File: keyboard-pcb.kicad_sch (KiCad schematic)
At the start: 24 parts, among them J1 Conn_01x05, J2 USB_C_Receptacle_USB2.0_16P, SW1 BOOT, SW2 RESET, U1 STM32F072CBTx, U2 74AHCT1G125, U3 XC6206PxxxMR

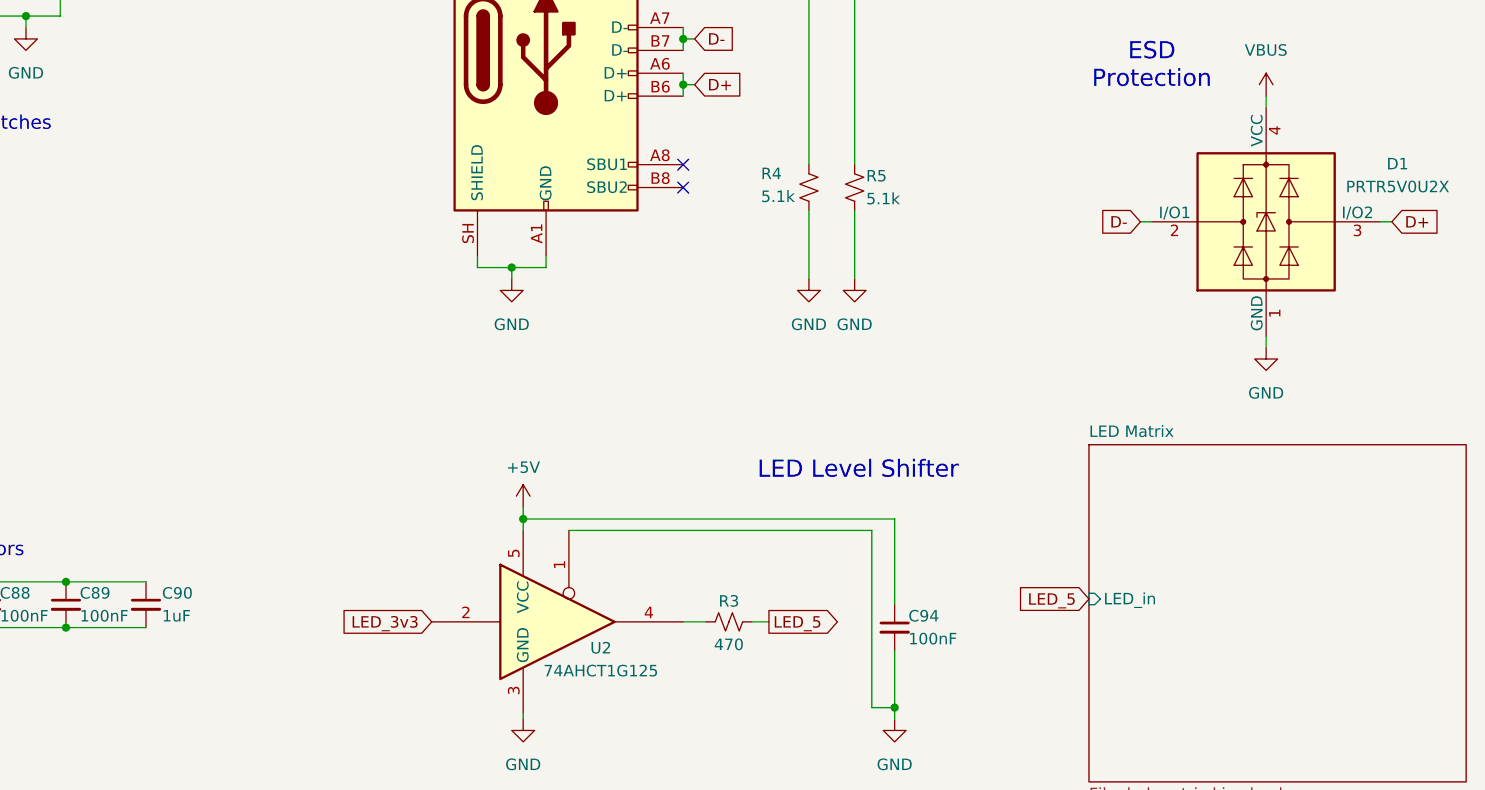
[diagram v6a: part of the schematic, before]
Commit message: usb and ldo routing
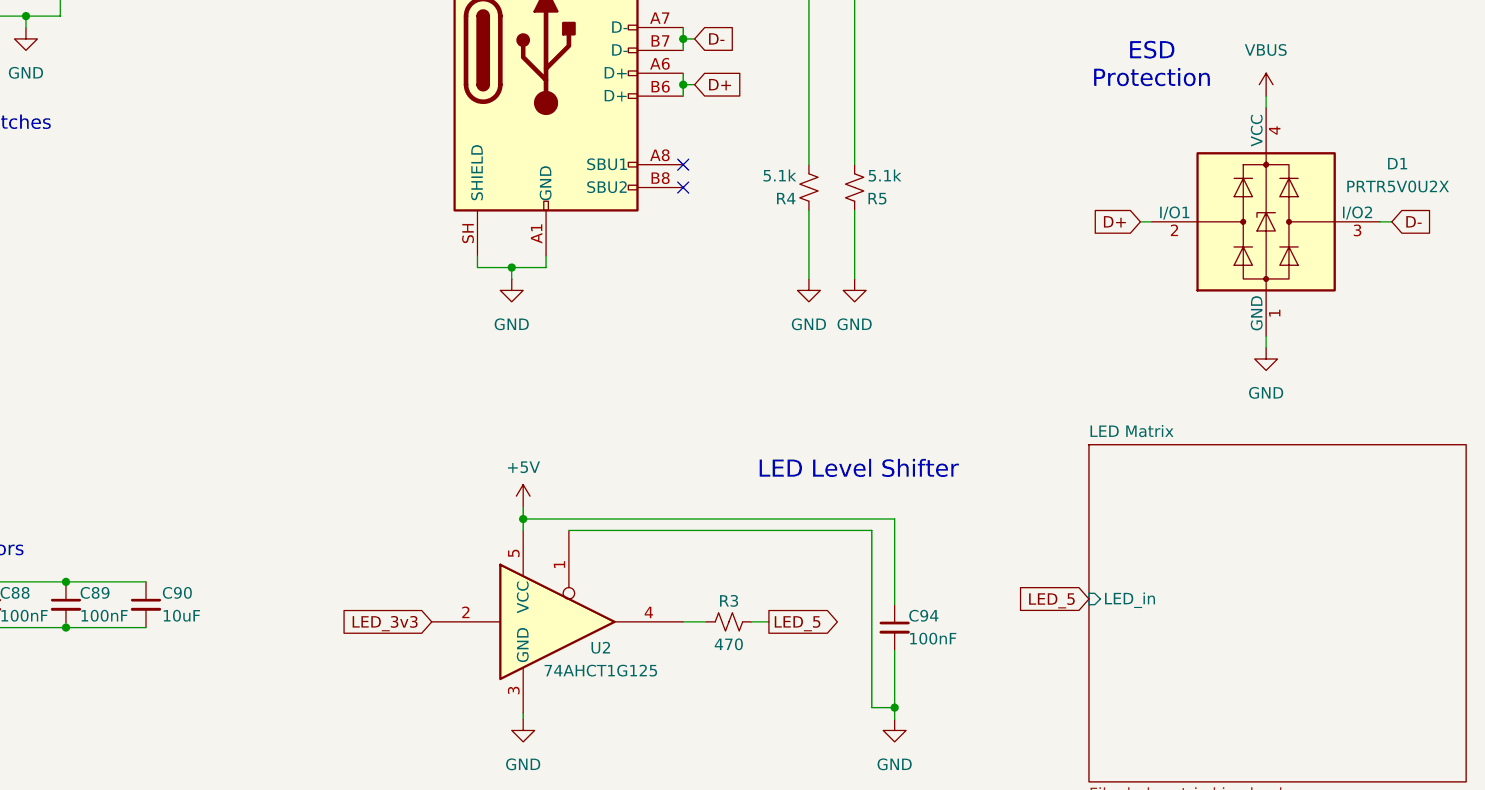
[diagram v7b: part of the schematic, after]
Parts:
- C90: value 1uF -> 10uF
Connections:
- net D+: now also D1.2 (I/O1); no longer D1.3 (I/O2)
- net D-: now also D1.3 (I/O2); no longer D1.2 (I/O1)
- net GND: now also R4.2, R5.1; no longer R4.1, R5.2
- net at J2.A5 (CC1): now also R5.2; no longer R5.1
- net at J2.B5 (CC2): now also R4.1; no longer R4.2
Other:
- moved on the sheet: R4, R5
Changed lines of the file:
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@@
 	(global_label "D-"
 		(shape input)
-		(at 247.015 66.04 180)
-		(fields_autoplaced yes)
-		(effects
-			(font
-				(size 1.27 1.27)
-			)
-			(justify right)
-		)
-		(property "Intersheetrefs" "${INTERSHEET_REFS}"
-			(at 241.1874 66.04 0)
-			(hide yes)
-			(show_name no)
-			(do_not_autoplace no)
-			(effects
-				(font
-					(size 1.27 1.27)
-				)
-				(justify right)
+		(at 274.955 66.04 0)
+		(fields_autoplaced yes)
+		(effects
+			(font
+				(size 1.27 1.27)
+			)
+			(justify left)
+		)
+		(property "Intersheetrefs" "${INTERSHEET_REFS}"
+			(at 280.7826 66.04 0)
+			(hide yes)
+			(show_name no)
+			(do_not_autoplace no)
+			(effects
+				(font
+					(size 1.27 1.27)
+				)
+				(justify left)
 			)
 		)
@@
 	(global_label "D+"
 		(shape input)
-		(at 274.955 66.04 0)
-		(fields_autoplaced yes)
-		(effects
-			(font
-				(size 1.27 1.27)
-			)
-			(justify left)
-		)
-		(property "Intersheetrefs" "${INTERSHEET_REFS}"
-			(at 280.7826 66.04 0)
-			(hide yes)
-			(show_name no)
-			(do_not_autoplace no)
-			(effects
-				(font
-					(size 1.27 1.27)
-				)
-				(justify left)
+		(at 247.015 66.04 180)
+		(fields_autoplaced yes)
+		(effects
+			(font
+				(size 1.27 1.27)
+			)
+			(justify right)
+		)
+		(property "Intersheetrefs" "${INTERSHEET_REFS}"
+			(at 241.1874 66.04 0)
+			(hide yes)
+			(show_name no)
+			(do_not_autoplace no)
+			(effects
+				(font
+					(size 1.27 1.27)
+				)
+				(justify right)
 			)
 		)
@@
 	(symbol
 		(lib_id "Device:R_Small_US")
-		(at 215.265 62.23 0)
+		(at 215.265 62.23 180)
 		(unit 1)
 		(body_style 1)
@@
 		(dnp no)
 		(property "Reference" "R5"
-			(at 216.535 60.96 0)
+			(at 218.948 63.5 0)
 			(show_name no)
 			(do_not_autoplace no)
@@
 		)
 		(property "Value" "5.1k"
-			(at 216.535 63.5 0)
+			(at 220.472 60.96 0)
 			(show_name no)
 			(do_not_autoplace no)
@@
 	(symbol
 		(lib_id "Device:R_Small_US")
-		(at 210.185 62.23 180)
+		(at 210.185 62.23 0)
 		(unit 1)
 		(body_style 1)
@@
 		(dnp no)
 		(property "Reference" "R4"
-			(at 204.851 60.706 0)
+			(at 208.788 63.5 0)
 			(show_name no)
 			(do_not_autoplace no)
@@
 		)
 		(property "Value" "5.1k"
-			(at 204.851 63.246 0)
+			(at 208.788 60.96 0)
 			(show_name no)
 			(do_not_autoplace no)
@@
 			)
 		)
-		(property "Value" "1uF"
+		(property "Value" "10uF"
 			(at 138.303 109.855 0)
 			(show_name no)

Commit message: completed pcb design
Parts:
- added H1, H2, H3, H4, H5: MountingHole_Pad, MountingHole:MountingHole_3.2mm_M3_DIN965_Pad, symbol Mechanical:MountingHole_Pad
- C85, C86, C87, C88, C89, C91, C94: footprint Capacitor_SMD:C_0402_1005Metric -> smd_silkscreen:C_0402_1005Metric
- R1, R2, R3, R4, R5: footprint Resistor_SMD:R_0402_1005Metric -> smd_silkscreen:R_0402_1005Metric
- renumbered SW1 to BOOT1, SW2 to RST1
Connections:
- net RST is gone; now on net NRST: J1.4 (Pin_4)
- net LED_3v3: now also U1.45 (PB8)
- net col6: now also U1.11 (PA1); no longer U1.13 (PA3)
- net col7: now also U1.12 (PA2); no longer U1.14 (PA4)
- net row0: now also U1.17 (PA7)
- net row1: now also U1.18 (PB0)
- net row2: now also U1.19 (PB1)
- net row3: now also U1.20 (PB2)
- net row4: now also U1.22 (PB11)
- net row5: now also U1.21 (PB10)
- no-connect marks 2 -> 13
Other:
- note added: "Mounting Holes"
